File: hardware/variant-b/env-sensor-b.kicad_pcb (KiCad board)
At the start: 4 copper layers, 28 x 51 mm, 58 parts, among them J1 USB-C 16P, J2 JST-PH 2P, SW1 SW_PROV, U1 ESP32-C6-MINI-1-N4, U2 SHT45-AD1F, U3 TPS62840DLC, U4 BQ24074RGTR, U5 USBLC6-2SC6

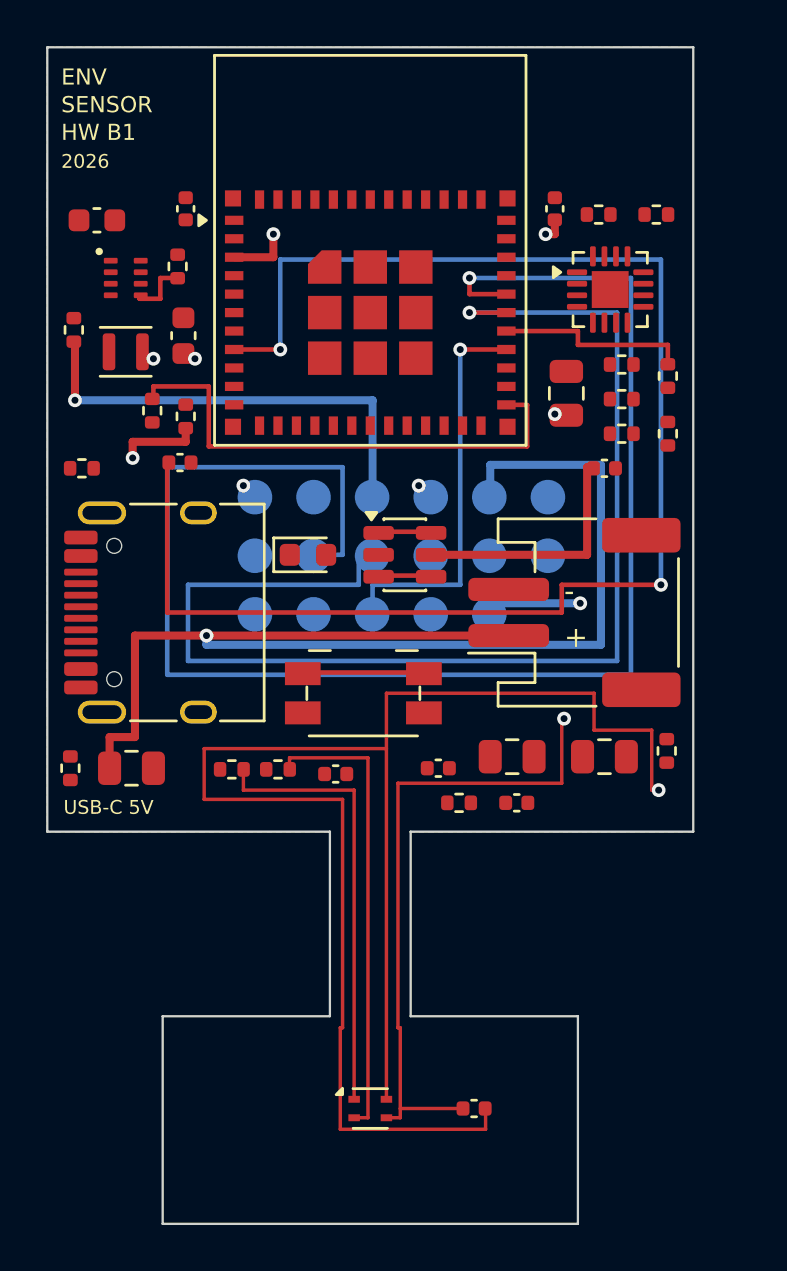
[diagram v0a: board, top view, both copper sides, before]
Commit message: chore(hw): regenerate both boards and previews after review fixes
Emit shared electrical corrections, validated routing and strengthened rules. Development allowances: A54/B58 unrouted and A6/B10 warnings per e584c6a; zero errors and parity differences. Preserve native KiCad SVG formatting. These are draft boards.
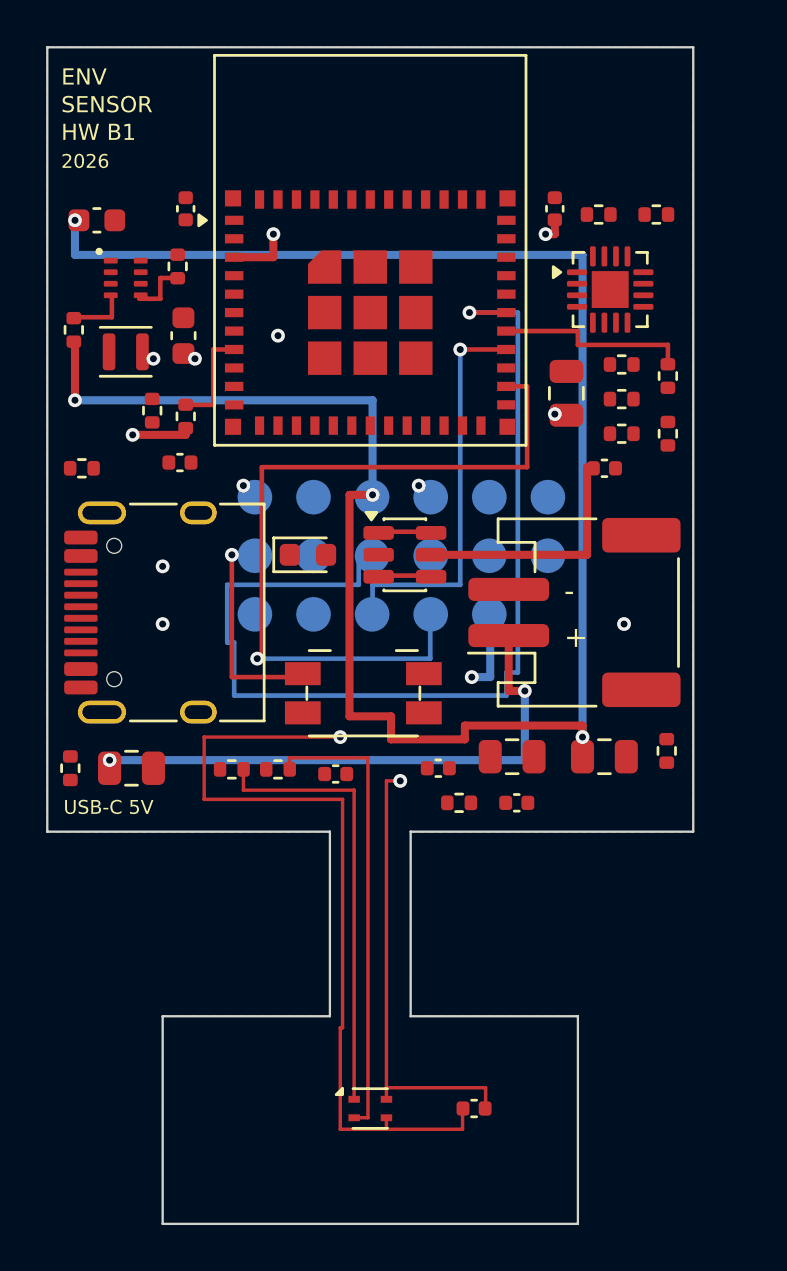
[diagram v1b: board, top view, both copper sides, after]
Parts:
- R6: value 52k3 1% -> 267k 1%
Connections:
- D1 pad 1: LED_A -> LED_N
- D1 pad 2: GND -> LED_A
- R2 pad 1: LED_A -> +3V0
- R2 pad 2: LED_N -> LED_A
- R5 pad 2: VSYS -> EN_REG
- U3 pad 4: VSYS -> EN_REG
- U4 pad 14: GND -> unconnected-(U4-TMR-Pad14)
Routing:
- net UART_TX: track 68.3 -> 0.00 mm, vias 1 -> 0
- net VSYS: track 19.7 -> 87.9 mm, vias 1 -> 4
- net EN: track 65.7 -> 4.50 mm, vias 2 -> 0
- net GND: track 76.7 -> 24.1 mm, vias 3 -> 7
- net TEST_MODE: track 0.00 -> 33.8 mm, vias 0 -> 1
- net VBAT: track 54.5 -> 24.4 mm, vias 1 -> 2
- net LED_N: track 22.0 -> 0.00 mm
- net UART_RX: track 54.3 -> 45.3 mm
- net +3V0: track 38.2 -> 45.0 mm
- net BTN_PROV: track 5.20 -> 9.60 mm, vias 0 -> 1
- net EN_REG: track 0.00 -> 2.60 mm

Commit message: chore(hw): regenerate both variants for power architecture
Regenerate the shared schematic, both PCB layouts, symbol library, BOM, netlist, enclosure parameters, cost reports and floorplan previews from the updated electrical platform.

Record the reviewed KiCad 10 development budget: zero errors and parity differences, with 59 unrouted items on A and 60 on B. These artifacts remain non-release drafts.
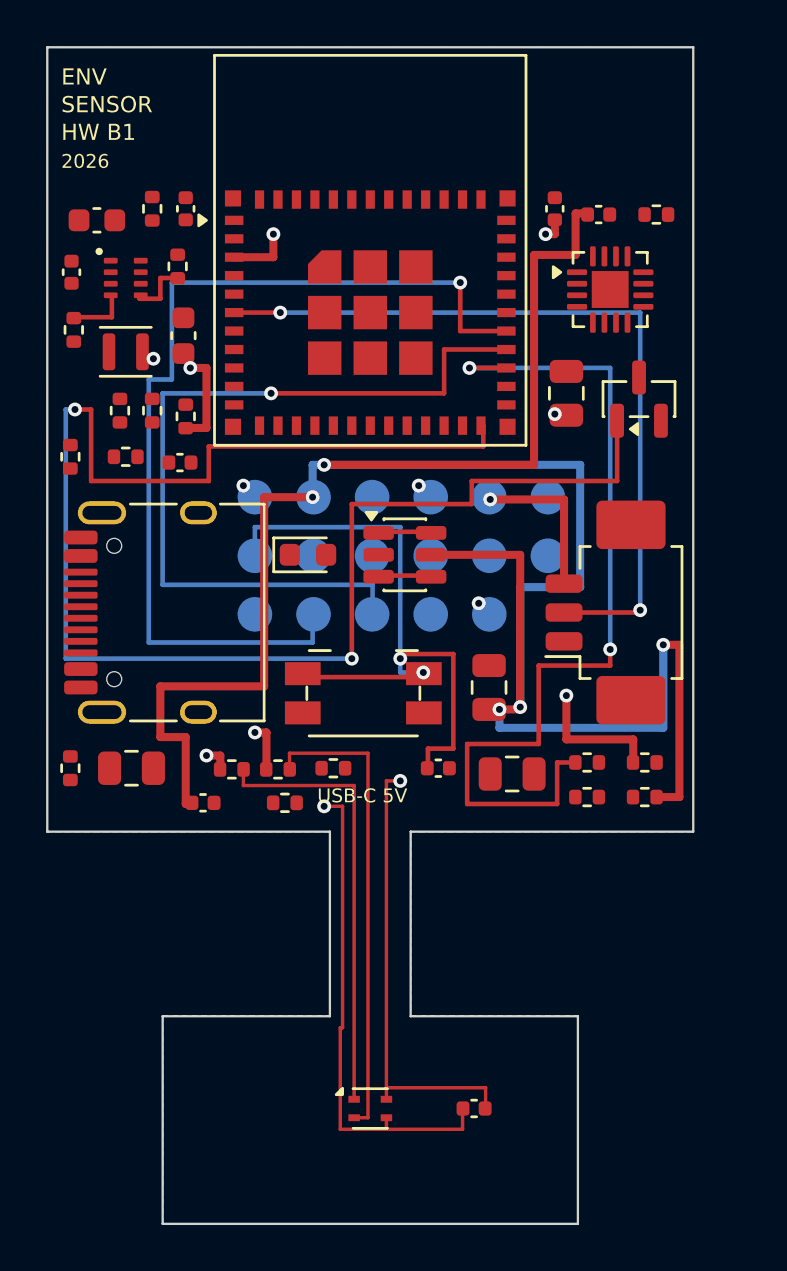
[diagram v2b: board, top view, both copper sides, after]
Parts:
- added Q1: 2N7002, sensorly:SOT-23, F.Cu at (125.7, 75.2)
- added R18: 47k 1%, sensorly:R_0402_1005Metric, F.Cu at (125.9, 92.5)
- J2: value JST-PH 2P -> Molex PicoBlade 3P; footprint sensorly:JST_PH_S2B-PH-SM4-TB_1x02-1MP_P2.00mm_Horizontal -> sensorly:Molex_PicoBlade_53261-0371_1x03-1MP_P1.25mm_Horizontal
- R11: value 3k09 1% -> 8k00 1%
- R13: value 3k57 1% -> 4k42 1%
- R7: value 10k 1% -> 100k 1%
- moved C13 30.0 mm to (101.0, 69.8), turned to 90 degrees
- moved R15 29.0 mm to (104.5, 67.0), turned to 90 degrees
- moved R9 23.8 mm to (125.9, 91.0)
- moved R10 22.3 mm to (112.4, 91.2), turned to 0 degrees
- moved R12 21.8 mm to (103.2, 75.8), turned to 90 degrees
- moved R11 21.6 mm to (103.4, 77.8)
- moved C10 20.5 mm to (103.7, 91.2)
- moved R8 17.3 mm to (123.4, 91.0)
- moved R14 16.7 mm to (110.3, 92.8), turned to 0 degrees
- moved C11 16.5 mm to (120.2, 91.5)
- moved R13 16.1 mm to (123.4, 92.5), turned to 0 degrees
- moved C12 11.0 mm to (123.9, 67.2)
- moved C14 5.88 mm to (106.8, 92.8)
- moved C9 3.16 mm to (119.2, 87.8), turned to 90 degrees
- moved R7 2.50 mm to (126.4, 67.2)
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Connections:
- J2 pad 1: VBAT -> GND
- J2 pad 2: GND -> PACK_TS
- J2 pad MP: GND -> unconnected-(J2-MountPin-PadMP)
- R7 pad 1: TS -> CHARGE_ENABLE
- R8 pad 1: VBUS -> USB_ISEL
- R8 pad 2: EN2 -> GND
- U1 pad 24: unconnected-(U1-IO18-Pad24) -> CHARGE_ENABLE
- U1 pad 27: unconnected-(U1-IO21-Pad27) -> USB_ISEL
- U1 pad 6: unconnected-(U1-IO3-Pad6) -> PACK_TS
- U4 pad 1: TS -> PACK_TS
- U4 pad 4: GND -> CHARGE_EN_N
- U4 pad 5: EN2 -> GND
- U4 pad 6: GND -> USB_ISEL
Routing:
- net VBUS: track 10.9 -> 101.5 mm, vias 0 -> 5
- net VSYS: track 87.9 -> 0.00 mm, vias 4 -> 0
- net CHARGE_ENABLE: track 0.00 -> 68.7 mm, vias 0 -> 2
- net UART_RX: track 45.3 -> 0.00 mm, vias 1 -> 0
- net USB_ISEL: track 0.00 -> 39.3 mm, vias 0 -> 2
- net PACK_TS: track 0.00 -> 33.9 mm, vias 0 -> 2
- net TEST_MODE: track 33.8 -> 0.00 mm, vias 1 -> 0
- net CHG_N: track 8.40 -> 41.5 mm, vias 0 -> 1
- net BTN_PROV: track 9.60 -> 28.9 mm, vias 1 -> 2
- net PG_N: track 17.3 -> 35.5 mm
- net VBAT: track 24.4 -> 6.80 mm, vias 2 -> 1
- net EN: track 4.50 -> 0.00 mm
- net +3V0: track 45.0 -> 40.9 mm, vias 8 -> 10
- net GND: track 24.1 -> 21.6 mm, vias 7 -> 3
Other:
- board text added: "- T +"
- board text removed: "+"
- board text removed: "-"

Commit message: chore(hw): regenerate the controlled prototype checkpoint
Regenerate shared schematic/BOM/netlist, both PCB projects/rules and floorplan SVGs from the electrical, library and routing corrections in 3c343e2, 135b78b, d863f52, 7802bdf, 0852837 and 7206b19. Preserve R21 DNP and the common A/B electrical platform.

Fresh KiCad 10.0.6: zero ERC violations; both boards have zero DRC errors, warnings and schematic parity differences, with no ignored checks. Development routing exception: A59/B52 unconnected items remain, explicitly recorded in the budget; all old warning allowances are removed. Prototype and product manufacturing gates still require complete routing and real qualification evidence. Full committed-source pipeline follows before push.
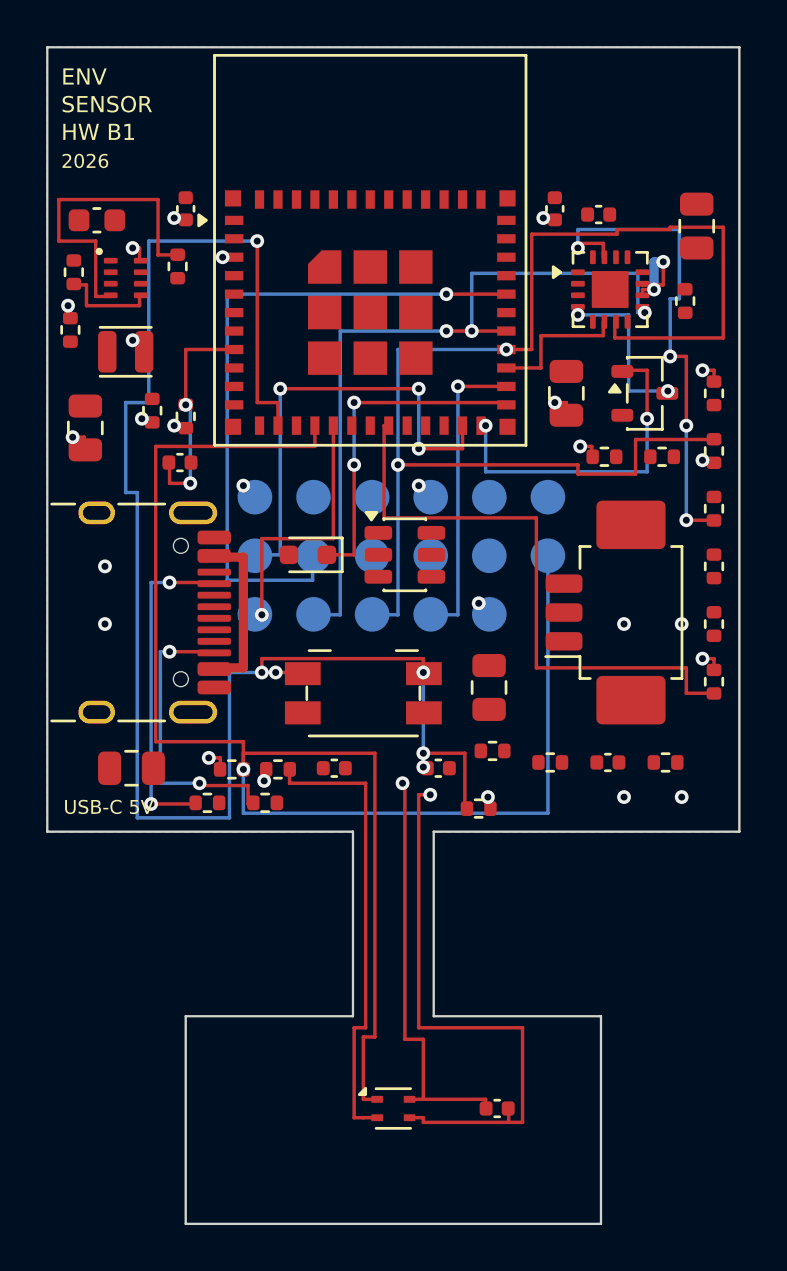
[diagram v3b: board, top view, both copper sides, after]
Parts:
- added R19: 100k 1%, sensorly:R_0402_1005Metric, F.Cu at (118.7, 93.0)
- added R20: 100k 1%, sensorly:R_0402_1005Metric, F.Cu at (128.9, 87.5)
- added R21: 0R, sensorly:R_0402_1005Metric, F.Cu at (126.8, 91.0)
- added R22: 10k 1%, sensorly:R_0402_1005Metric, F.Cu at (101.0, 72.2)
- C1: value 22uF/6.3V X5R -> 10uF/16V X5R
- C10, C11: value 10uF/6.3V X5R -> 10uF/16V X5R
- C3, C4: value 1uF/16V X7R -> 1uF/16V X5R
- C8: value 10uF/6.3V X5R -> 10uF/16V X5R; footprint sensorly:C_0603_1608Metric -> sensorly:C_0805_2012Metric
- D1: footprint sensorly:LED_0603_1608Metric -> sensorly:Kingbright_KP1608SGC
- L1: footprint sensorly:L_Murata_DFE201610P -> sensorly:L_Murata_DFE201612E
- Q1: footprint sensorly:SOT-23 -> sensorly:Onsemi_CASE318_SOT23
- R11: value 8k00 1% -> 8k06 1%
- TP10: value USB_DP -> USB_D_P
- TP11: value USB_DM -> USB_D_N
- TP7: value BTN_PROV -> BOOT_N
- U4: footprint sensorly:VQFN-16-1EP_3x3mm_P0.5mm_EP1.6x1.6mm -> sensorly:TI_RGT0016B_VQFN16_3x3mm
- U5: footprint sensorly:SOT-23-6 -> sensorly:ST_USBLC6_SOT23_6
- moved C13 31.5 mm to (124.3, 91.0), turned to 0 degrees
- moved R15 29.6 mm to (121.8, 91.0), turned to 0 degrees
- moved R12 26.1 mm to (128.9, 80.0)
- moved R11 23.2 mm to (126.7, 77.8)
- moved C9 21.9 mm to (128.2, 67.8)
- moved R10 17.9 mm to (124.2, 77.8)
- moved R8 16.9 mm to (128.9, 75.0), turned to 90 degrees
- moved C11 16.5 mm to (103.7, 91.2)
- moved R16 16.1 mm to (106.9, 92.8), turned to 0 degrees
- moved C10 15.9 mm to (119.2, 87.8), turned to 90 degrees
- moved R9 13.8 mm to (128.9, 77.5), turned to 90 degrees
- moved R13 11.4 mm to (128.9, 82.5), turned to 90 degrees
- moved R14 9.28 mm to (119.3, 90.5)
- moved R17 8.57 mm to (109.4, 92.8), turned to 0 degrees
- moved R18 8.08 mm to (128.9, 85.0), turned to 90 degrees
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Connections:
- net USB_DM renamed USB_D_N
- net USB_DP renamed USB_D_P
- D1 pad 1: LED_N -> LED_A
- D1 pad 2: LED_A -> LED_N
- R8 pad 2: GND -> +3V0
- TP7 pad 1: BTN_PROV -> BOOT_N
- U1 pad 13: unconnected-(U1-IO1-Pad13) -> BTN_PROV
- U1 pad 19: unconnected-(U1-IO14-Pad19) -> USB_EN2
- U1 pad 22: unconnected-(U1-IO8-Pad22) -> BOOT_MODE_H
- U1 pad 23: BTN_PROV -> BOOT_N
- U1 pad 6: PACK_TS -> PACK_TS_SENSE
- U4 pad 5: GND -> USB_EN2
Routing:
- net VBUS: track 101.5 -> 7.60 mm, vias 5 -> 0
- net SDA: track 19.1 -> 74.4 mm, vias 0 -> 1
- net CHARGE_ENABLE: track 68.7 -> 14.5 mm
- net BTN_PROV: track 28.9 -> 70.2 mm, vias 2 -> 6
- net PACK_TS: track 33.9 -> 0.00 mm, vias 2 -> 0
- net USB_ISEL: track 39.3 -> 6.20 mm, vias 2 -> 0
- net UART_TX: track 0.00 -> 29.3 mm, vias 0 -> 1
- net USB_EN2: track 0.00 -> 26.1 mm
- net PG_N: track 35.5 -> 57.8 mm, vias 1 -> 2
- net ITERM: track 0.00 -> 22.0 mm, vias 0 -> 4
- net BOOT_N: track 0.00 -> 19.8 mm, vias 0 -> 3
- net LED_N: track 0.00 -> 14.5 mm, vias 0 -> 2
- net CC1: track 0.00 -> 14.2 mm, vias 0 -> 2
- net TEST_MODE: track 0.00 -> 13.2 mm, vias 0 -> 1
- net CC2: track 0.00 -> 12.9 mm, vias 0 -> 2
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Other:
- board size 28 x 51 mm -> 30 x 51 mm
- board text added: "J2 1- 2T 3+"
- board text removed: "- T +"

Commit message: build(boardgen): regenerate reviewed local power layouts
Regenerate both boards, rule areas, floorplan SVGs and enclosure parameters from 3109ac3. Preserve zero DRC errors/warnings/parity with A56/B49 unfinished connections; outputs remain draft engineering artifacts.
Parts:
- moved C11 26.7 mm to (124.0, 74.0)
- moved C10 19.5 mm to (128.2, 70.5)
- moved R2 19.4 mm to (118.5, 89.2)
- moved C1 19.3 mm to (104.9, 67.1), turned to 180 degrees
- moved C4 17.8 mm to (123.5, 76.5), turned to 90 degrees
- moved R16 15.5 mm to (101.4, 78.2)
- moved R12 11.7 mm to (119.2, 86.5), turned to 0 degrees
- moved R19 9.75 mm to (109.0, 92.8)
- moved C3 9.50 mm to (122.0, 76.5)
- moved R18 9.42 mm to (120.2, 88.5)
- moved C2 9.00 mm to (106.0, 76.0)
- moved C14 8.51 mm to (103.9, 90.8)
- moved R17 8.25 mm to (101.4, 90.8)
- moved R11 8.07 mm to (128.9, 85.5), turned to 90 degrees
- moved C12 7.27 mm to (127.2, 73.8)
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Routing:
- net VBAT: track 0.10 -> 57.6 mm, vias 0 -> 6
- net VBAT_SENSE: track 0.00 -> 52.9 mm, vias 0 -> 2
- net TEST_MODE: track 13.2 -> 43.4 mm, vias 1 -> 3
- net ISET: track 0.20 -> 30.1 mm, vias 0 -> 2
- net BTN_PROV: track 70.2 -> 43.9 mm
- net ITERM: track 22.0 -> 44.7 mm
- net BOOT_N: track 19.8 -> 0.00 mm, vias 3 -> 0
- net CHG_N: track 32.8 -> 49.3 mm, vias 3 -> 4
- net PG_N: track 57.8 -> 42.6 mm, vias 2 -> 3
- net LED_N: track 14.5 -> 0.00 mm, vias 2 -> 0
- net CC1: track 14.2 -> 0.00 mm, vias 2 -> 0
- net EN_REG: track 14.0 -> 0.00 mm
- net CC2: track 12.9 -> 0.00 mm, vias 2 -> 0
- net USB_EN2: track 26.1 -> 38.3 mm
- net GND: track 20.3 -> 29.7 mm, vias 9 -> 21
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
